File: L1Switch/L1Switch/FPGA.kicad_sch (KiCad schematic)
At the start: 34 parts, among them J11 Conn_01x06_Male, U1 XC7A35T-FTG256, X1 LFSPXO076034CUTT

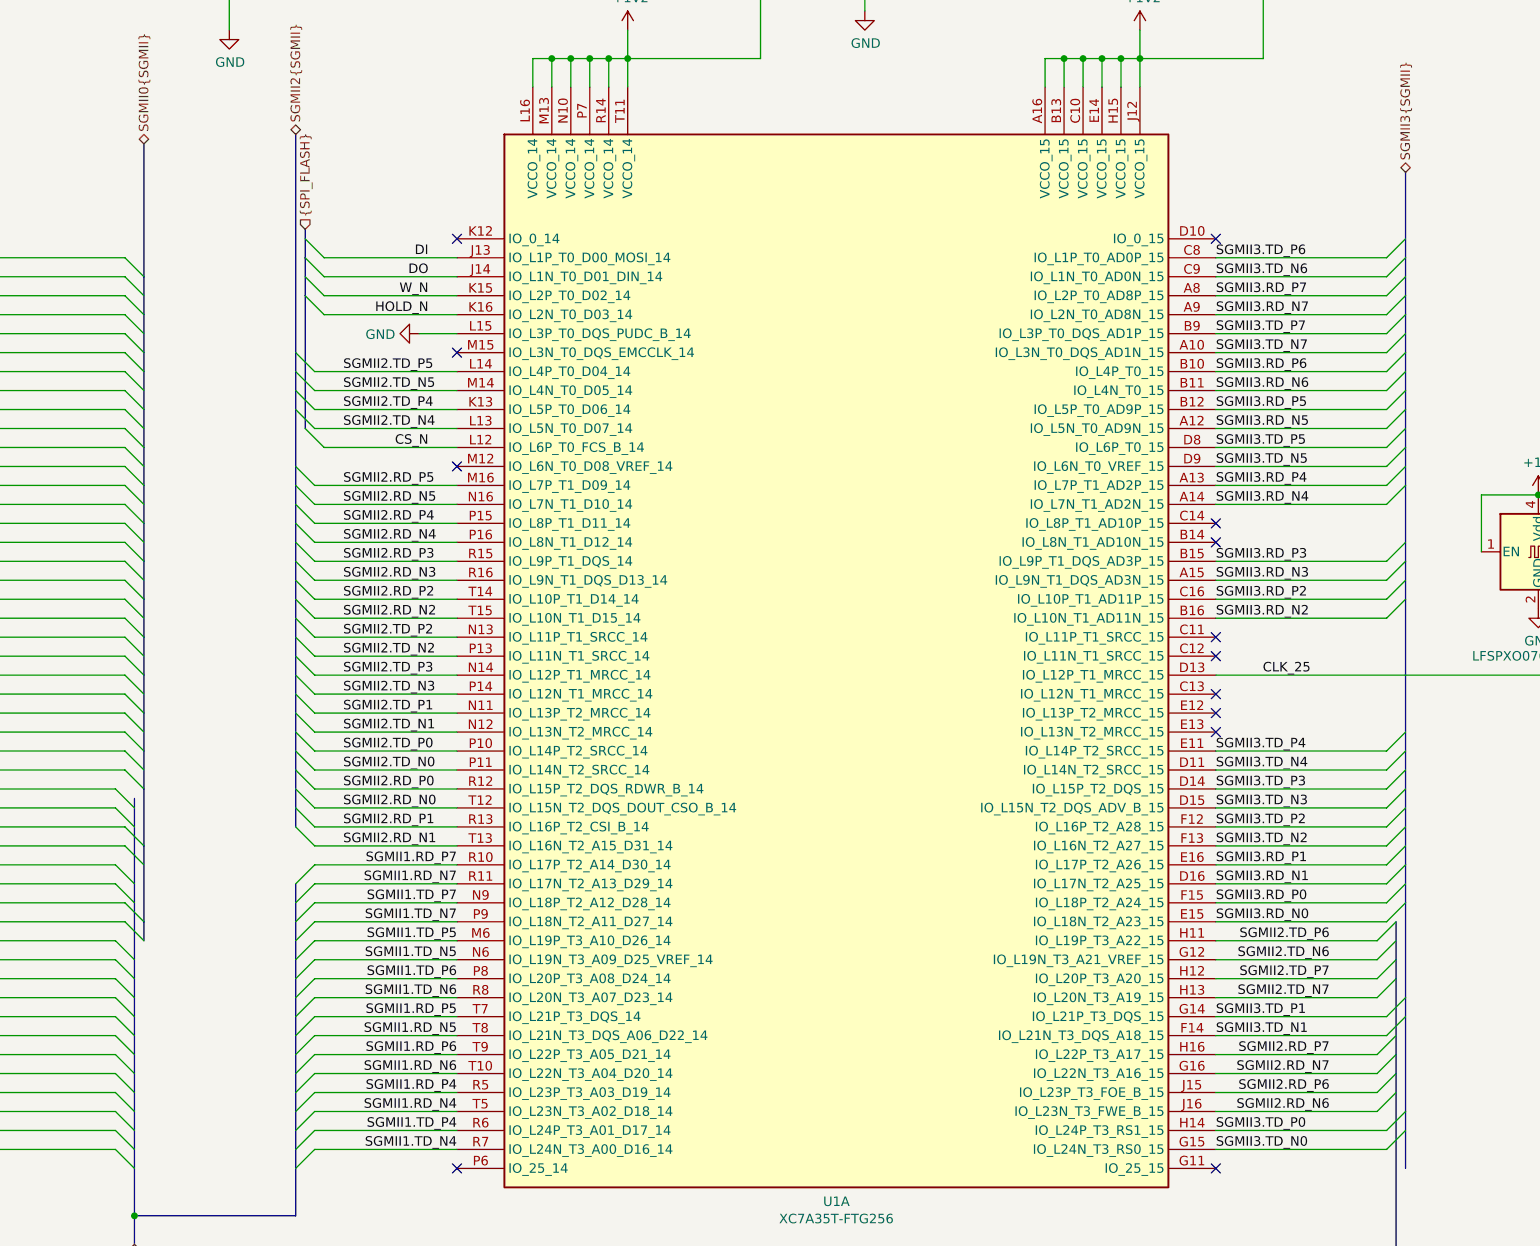
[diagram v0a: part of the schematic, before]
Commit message: Swap fan connector orientation. Add PU/PD for JTAG pins.
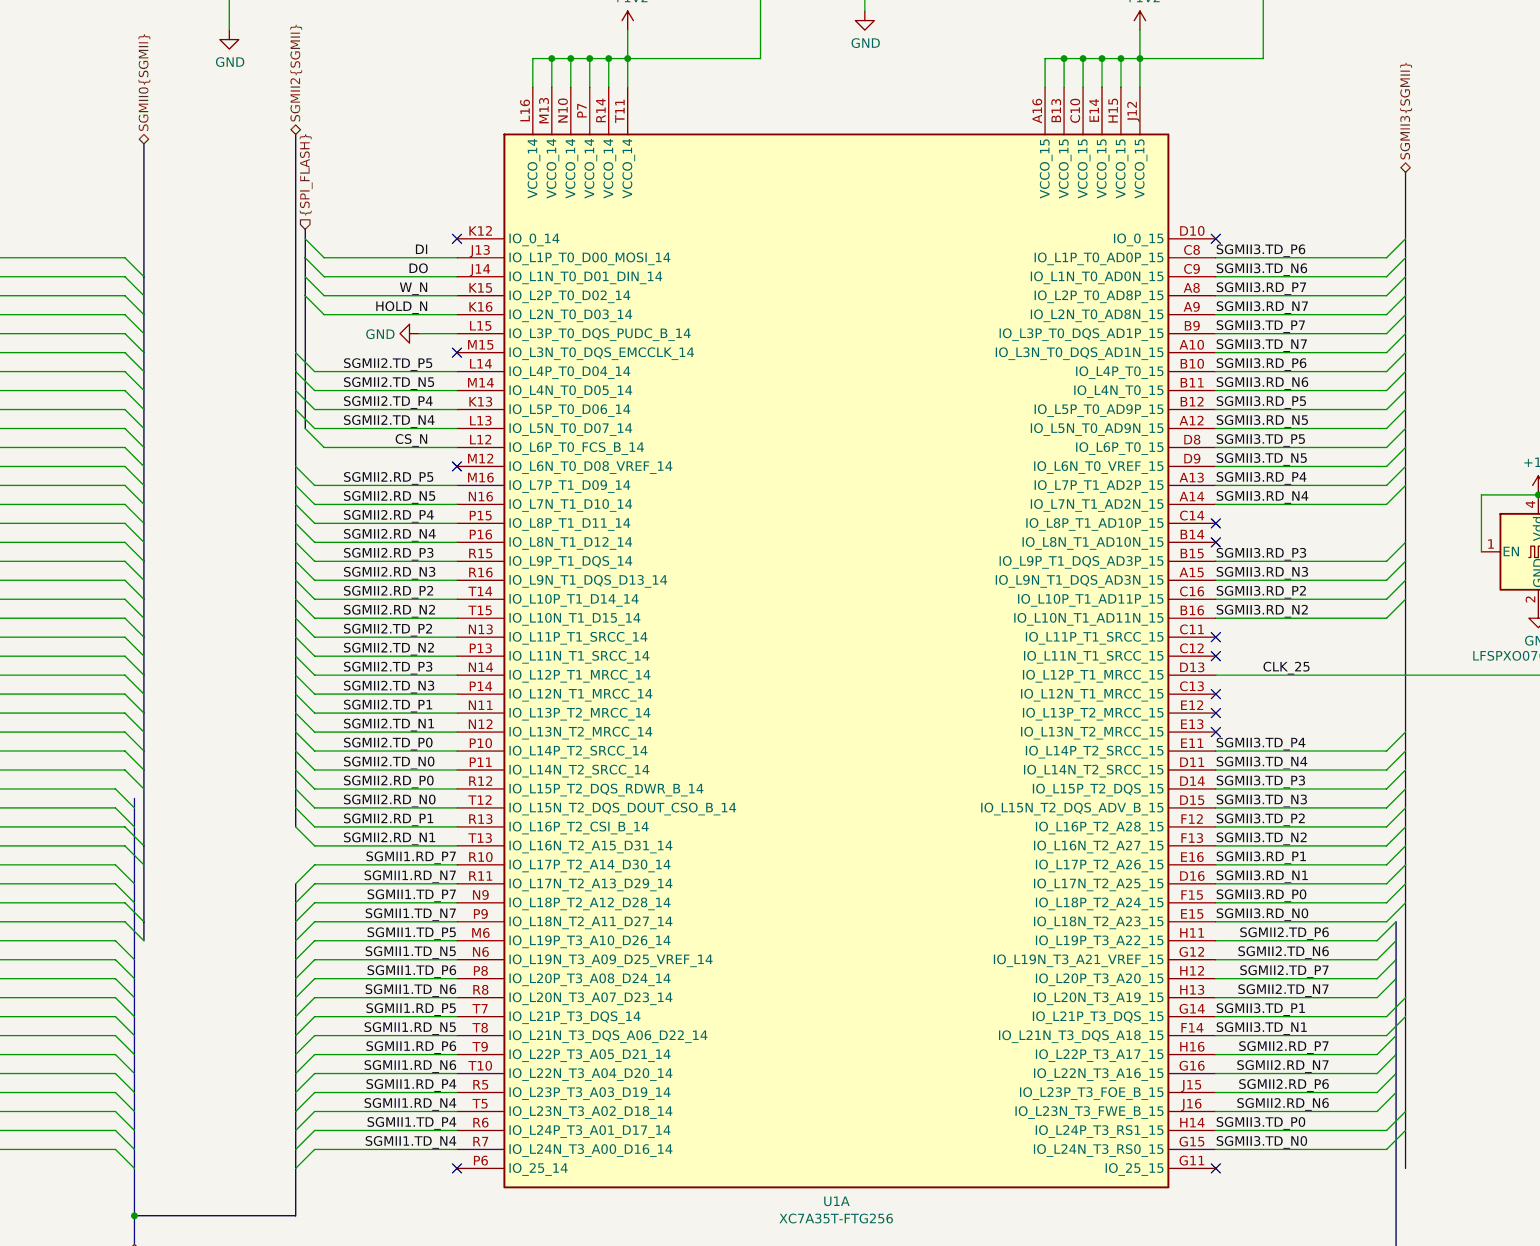
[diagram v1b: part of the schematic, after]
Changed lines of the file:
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@@
   (junction (at 414.02 125.73))
   (junction (at 213.36 198.12))
+  (no_connect (at 177.8 191.77))
+  (no_connect (at 46.99 114.3))
+  (no_connect (at 76.2 107.95))
+  (no_connect (at 256.54 67.31))
+  (no_connect (at 256.54 82.55))
+  (no_connect (at 76.2 115.57))
+  (no_connect (at 358.14 128.27))
+  (no_connect (at 358.14 105.41))
+  (no_connect (at 76.2 102.87))
+  (no_connect (at 358.14 107.95))
+  (no_connect (at 358.14 191.77))
+  (no_connect (at 76.2 105.41))
+  (no_connect (at 46.99 124.46))
+  (no_connect (at 256.54 191.77))
+  (no_connect (at 358.14 130.81))
+  (no_connect (at 46.99 116.84))
+  (no_connect (at 358.14 123.19))
+  (no_connect (at 358.14 120.65))
+  (no_connect (at 358.14 133.35))
+  (no_connect (at 358.14 67.31))
+  (no_connect (at 256.54 97.79))
   (no_connect (at 177.8 67.31))
-  (no_connect (at 358.14 128.27))
-  (no_connect (at 76.2 102.87))
-  (no_connect (at 76.2 105.41))
-  (no_connect (at 256.54 67.31))
-  (no_connect (at 76.2 107.95))
-  (no_connect (at 358.14 105.41))
-  (no_connect (at 46.99 114.3))
-  (no_connect (at 76.2 115.57))
-  (no_connect (at 358.14 133.35))
-  (no_connect (at 358.14 120.65))
-  (no_connect (at 256.54 82.55))
-  (no_connect (at 358.14 123.19))
-  (no_connect (at 256.54 191.77))
-  (no_connect (at 46.99 116.84))
-  (no_connect (at 46.99 124.46))
-  (no_connect (at 358.14 107.95))
-  (no_connect (at 358.14 130.81))
-  (no_connect (at 358.14 191.77))
-  (no_connect (at 177.8 191.77))
-  (no_connect (at 256.54 97.79))
-  (no_connect (at 358.14 67.31))
   (bus_entry (at 210.82 140.97) (size 2.54 2.54))
   (bus_entry (at 210.82 143.51) (size 2.54 2.54))
@@
     (stroke (width 0) (type solid) (color 0 0 0 0))
   )
-  (bus (pts (xy 213.36 171.45) (xy 213.36 173.99))
-    (stroke (width 0) (type solid) (color 0 0 0 0))
-  )
-  (bus (pts (xy 213.36 173.99) (xy 213.36 179.07))
-    (stroke (width 0) (type solid) (color 0 0 0 0))
-  )
-  (bus (pts (xy 213.36 179.07) (xy 213.36 184.15))
+  (bus (pts (xy 213.36 171.45) (xy 213.36 176.53))
+    (stroke (width 0) (type solid) (color 0 0 0 0))
+  )
+  (bus (pts (xy 213.36 176.53) (xy 213.36 181.61))
+    (stroke (width 0) (type solid) (color 0 0 0 0))
+  )
+  (bus (pts (xy 213.36 181.61) (xy 213.36 184.15))
     (stroke (width 0) (type solid) (color 0 0 0 0))
   )
@@
     (stroke (width 0) (type solid) (color 0 0 0 0))
   )
-  (bus (pts (xy 214.63 135.89) (xy 214.63 140.97))
-    (stroke (width 0) (type solid) (color 0 0 0 0))
-  )
-  (bus (pts (xy 214.63 140.97) (xy 214.63 148.59))
+  (bus (pts (xy 214.63 135.89) (xy 214.63 138.43))
+    (stroke (width 0) (type solid) (color 0 0 0 0))
+  )
+  (bus (pts (xy 214.63 138.43) (xy 214.63 148.59))
     (stroke (width 0) (type solid) (color 0 0 0 0))
   )
@@
     (stroke (width 0) (type solid) (color 0 0 0 0))
   )
-  (bus (pts (xy 234.95 53.34) (xy 234.95 82.55))
-    (stroke (width 0) (type solid) (color 0 0 0 0))
-  )
-  (bus (pts (xy 234.95 82.55) (xy 234.95 87.63))
-    (stroke (width 0) (type solid) (color 0 0 0 0))
-  )
-  (bus (pts (xy 234.95 87.63) (xy 234.95 97.79))
-    (stroke (width 0) (type solid) (color 0 0 0 0))
-  )
-  (bus (pts (xy 234.95 97.79) (xy 234.95 100.33))
-    (stroke (width 0) (type solid) (color 0 0 0 0))
-  )
-  (bus (pts (xy 234.95 100.33) (xy 234.95 105.41))
-    (stroke (width 0) (type solid) (color 0 0 0 0))
-  )
-  (bus (pts (xy 234.95 105.41) (xy 234.95 110.49))
-    (stroke (width 0) (type solid) (color 0 0 0 0))
-  )
-  (bus (pts (xy 234.95 110.49) (xy 234.95 115.57))
-    (stroke (width 0) (type solid) (color 0 0 0 0))
-  )
-  (bus (pts (xy 234.95 115.57) (xy 234.95 120.65))
-    (stroke (width 0) (type solid) (color 0 0 0 0))
-  )
-  (bus (pts (xy 234.95 120.65) (xy 234.95 125.73))
-    (stroke (width 0) (type solid) (color 0 0 0 0))
-  )
-  (bus (pts (xy 234.95 125.73) (xy 234.95 130.81))
-    (stroke (width 0) (type solid) (color 0 0 0 0))
-  )
-  (bus (pts (xy 234.95 130.81) (xy 234.95 133.35))
-    (stroke (width 0) (type solid) (color 0 0 0 0))
-  )
-  (bus (pts (xy 234.95 133.35) (xy 234.95 138.43))
-    (stroke (width 0) (type solid) (color 0 0 0 0))
-  )
-  (bus (pts (xy 234.95 138.43) (xy 234.95 143.51))
-    (stroke (width 0) (type solid) (color 0 0 0 0))
-  )
-  (bus (pts (xy 234.95 143.51) (xy 234.95 146.05))
+  (bus (pts (xy 234.95 53.34) (xy 234.95 85.09))
+    (stroke (width 0) (type solid) (color 0 0 0 0))
+  )
+  (bus (pts (xy 234.95 85.09) (xy 234.95 90.17))
+    (stroke (width 0) (type solid) (color 0 0 0 0))
+  )
+  (bus (pts (xy 234.95 90.17) (xy 234.95 100.33))
+    (stroke (width 0) (type solid) (color 0 0 0 0))
+  )
+  (bus (pts (xy 234.95 100.33) (xy 234.95 102.87))
+    (stroke (width 0) (type solid) (color 0 0 0 0))
+  )
+  (bus (pts (xy 234.95 102.87) (xy 234.95 107.95))
+    (stroke (width 0) (type solid) (color 0 0 0 0))
+  )
+  (bus (pts (xy 234.95 107.95) (xy 234.95 113.03))
+    (stroke (width 0) (type solid) (color 0 0 0 0))
+  )
+  (bus (pts (xy 234.95 113.03) (xy 234.95 118.11))
+    (stroke (width 0) (type solid) (color 0 0 0 0))
+  )
+  (bus (pts (xy 234.95 118.11) (xy 234.95 123.19))
+    (stroke (width 0) (type solid) (color 0 0 0 0))
+  )
+  (bus (pts (xy 234.95 123.19) (xy 234.95 128.27))
+    (stroke (width 0) (type solid) (color 0 0 0 0))
+  )
+  (bus (pts (xy 234.95 128.27) (xy 234.95 133.35))
+    (stroke (width 0) (type solid) (color 0 0 0 0))
+  )
+  (bus (pts (xy 234.95 133.35) (xy 234.95 135.89))
+    (stroke (width 0) (type solid) (color 0 0 0 0))
+  )
+  (bus (pts (xy 234.95 135.89) (xy 234.95 140.97))
+    (stroke (width 0) (type solid) (color 0 0 0 0))
+  )
+  (bus (pts (xy 234.95 140.97) (xy 234.95 146.05))
     (stroke (width 0) (type solid) (color 0 0 0 0))
   )
@@
     (stroke (width 0) (type solid) (color 0 0 0 0))
   )
-  (bus (pts (xy 383.54 151.13) (xy 383.54 156.21))
-    (stroke (width 0) (type solid) (color 0 0 0 0))
-  )
-  (bus (pts (xy 383.54 156.21) (xy 383.54 168.91))
-    (stroke (width 0) (type solid) (color 0 0 0 0))
-  )
+  (bus (pts (xy 383.54 151.13) (xy 383.54 153.67))
+    (stroke (width 0) (type solid) (color 0 0 0 0))
+  )
+  (bus (pts (xy 383.54 153.67) (xy 383.54 168.91))
+    (stroke (width 0) (type solid) (color 0 0 0 0))
+  )

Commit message: Update RJ45 pinout on schematic and partial layout update.
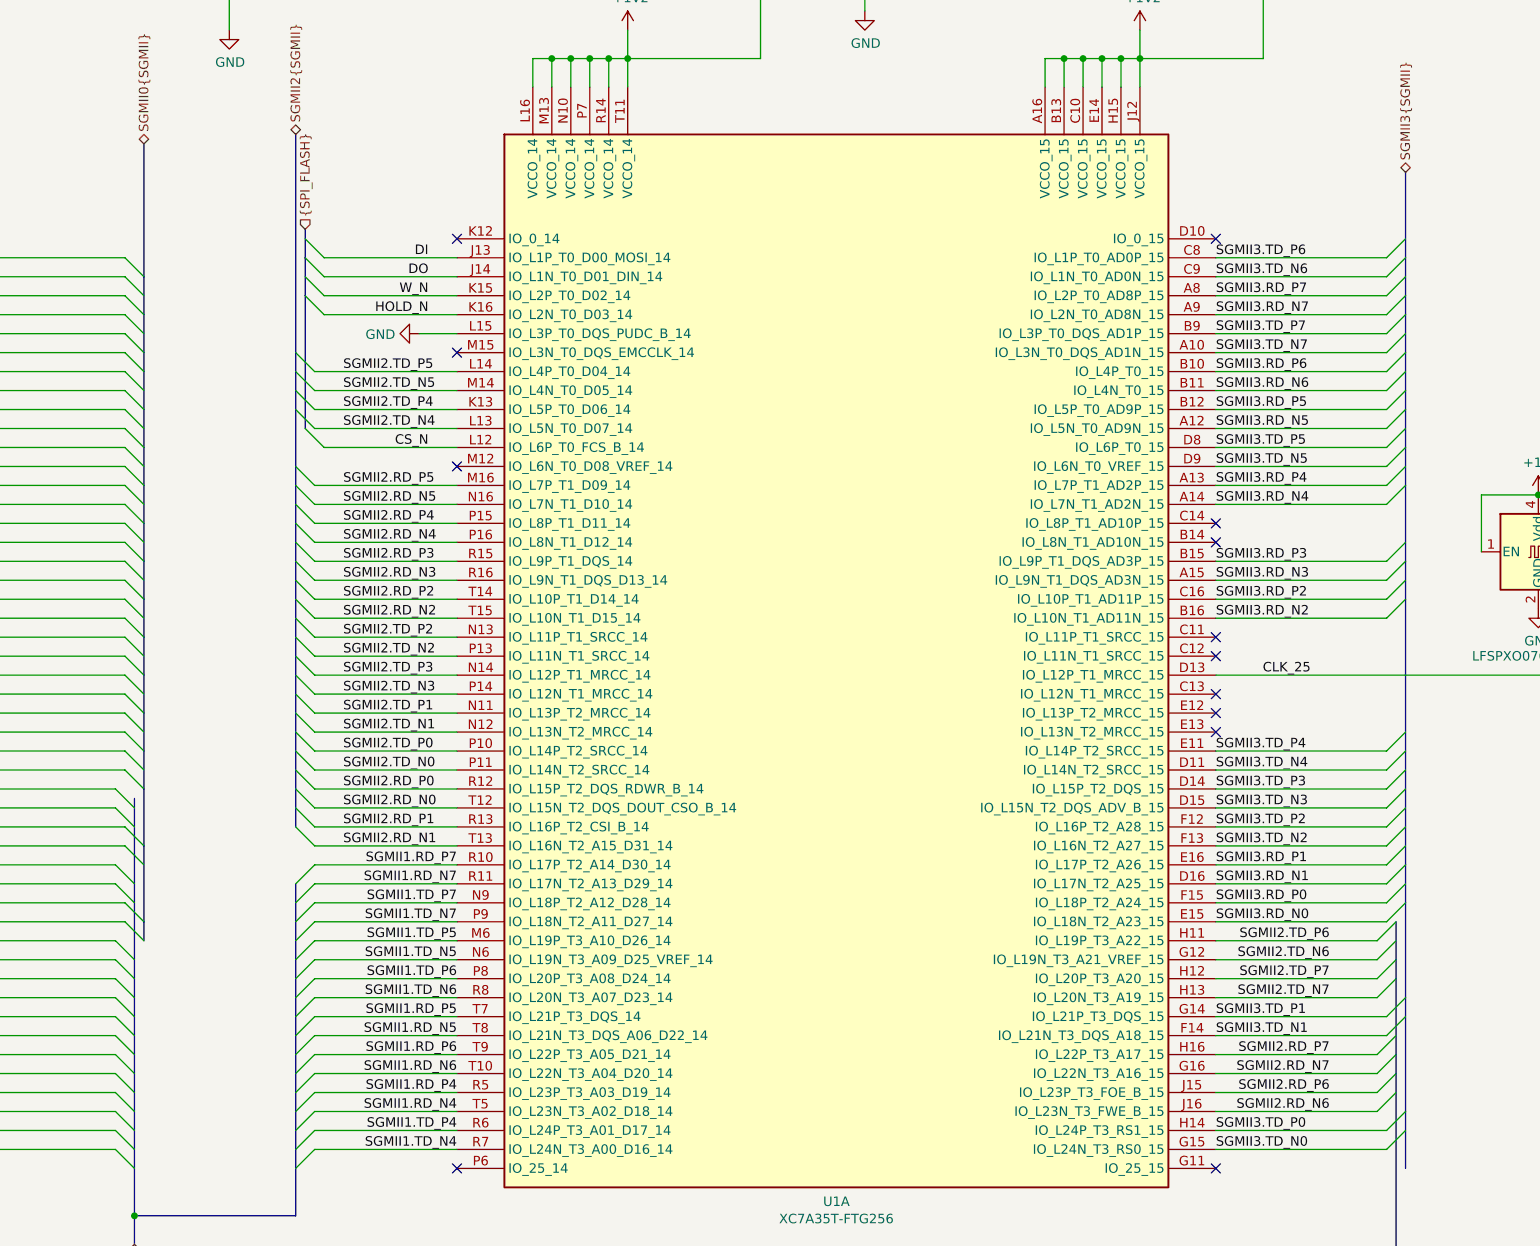
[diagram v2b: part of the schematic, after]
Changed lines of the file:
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@@
 (kicad_sch (version 20200608) (host eeschema "5.99.0-unknown-1973153~101~ubuntu20.04.1")
-  (page 2 12)
+  (page 1 12)
   (paper "B")
   (bus_alias "MAC1_SGMII" (members ))
@@
   (junction (at 414.02 125.73))
   (junction (at 213.36 198.12))
+  (no_connect (at 358.14 105.41))
+  (no_connect (at 358.14 123.19))
+  (no_connect (at 358.14 191.77))
+  (no_connect (at 76.2 102.87))
+  (no_connect (at 76.2 115.57))
+  (no_connect (at 177.8 67.31))
+  (no_connect (at 358.14 130.81))
+  (no_connect (at 256.54 67.31))
+  (no_connect (at 46.99 114.3))
+  (no_connect (at 358.14 133.35))
+  (no_connect (at 76.2 107.95))
+  (no_connect (at 358.14 120.65))
+  (no_connect (at 256.54 97.79))
   (no_connect (at 177.8 191.77))
-  (no_connect (at 46.99 114.3))
-  (no_connect (at 76.2 107.95))
-  (no_connect (at 256.54 67.31))
+  (no_connect (at 256.54 191.77))
+  (no_connect (at 76.2 105.41))
+  (no_connect (at 46.99 116.84))
+  (no_connect (at 358.14 128.27))
+  (no_connect (at 358.14 67.31))
+  (no_connect (at 46.99 124.46))
   (no_connect (at 256.54 82.55))
-  (no_connect (at 76.2 115.57))
-  (no_connect (at 358.14 128.27))
-  (no_connect (at 358.14 105.41))
-  (no_connect (at 76.2 102.87))
   (no_connect (at 358.14 107.95))
-  (no_connect (at 358.14 191.77))
-  (no_connect (at 76.2 105.41))
-  (no_connect (at 46.99 124.46))
-  (no_connect (at 256.54 191.77))
-  (no_connect (at 358.14 130.81))
-  (no_connect (at 46.99 116.84))
-  (no_connect (at 358.14 123.19))
-  (no_connect (at 358.14 120.65))
-  (no_connect (at 358.14 133.35))
-  (no_connect (at 358.14 67.31))
-  (no_connect (at 256.54 97.79))
-  (no_connect (at 177.8 67.31))
   (bus_entry (at 210.82 140.97) (size 2.54 2.54))
   (bus_entry (at 210.82 143.51) (size 2.54 2.54))
@@
     (stroke (width 0) (type solid) (color 0 0 0 0))
   )
-  (bus (pts (xy 213.36 171.45) (xy 213.36 176.53))
-    (stroke (width 0) (type solid) (color 0 0 0 0))
-  )
-  (bus (pts (xy 213.36 176.53) (xy 213.36 181.61))
-    (stroke (width 0) (type solid) (color 0 0 0 0))
-  )
-  (bus (pts (xy 213.36 181.61) (xy 213.36 184.15))
+  (bus (pts (xy 213.36 171.45) (xy 213.36 173.99))
+    (stroke (width 0) (type solid) (color 0 0 0 0))
+  )
+  (bus (pts (xy 213.36 173.99) (xy 213.36 179.07))
+    (stroke (width 0) (type solid) (color 0 0 0 0))
+  )
+  (bus (pts (xy 213.36 179.07) (xy 213.36 184.15))
     (stroke (width 0) (type solid) (color 0 0 0 0))
   )
@@
     (stroke (width 0) (type solid) (color 0 0 0 0))
   )
-  (bus (pts (xy 214.63 135.89) (xy 214.63 138.43))
-    (stroke (width 0) (type solid) (color 0 0 0 0))
-  )
-  (bus (pts (xy 214.63 138.43) (xy 214.63 148.59))
+  (bus (pts (xy 214.63 135.89) (xy 214.63 140.97))
+    (stroke (width 0) (type solid) (color 0 0 0 0))
+  )
+  (bus (pts (xy 214.63 140.97) (xy 214.63 148.59))
     (stroke (width 0) (type solid) (color 0 0 0 0))
   )
@@
     (stroke (width 0) (type solid) (color 0 0 0 0))
   )
-  (bus (pts (xy 234.95 53.34) (xy 234.95 85.09))
-    (stroke (width 0) (type solid) (color 0 0 0 0))
-  )
-  (bus (pts (xy 234.95 85.09) (xy 234.95 90.17))
-    (stroke (width 0) (type solid) (color 0 0 0 0))
-  )
-  (bus (pts (xy 234.95 90.17) (xy 234.95 100.33))
-    (stroke (width 0) (type solid) (color 0 0 0 0))
-  )
-  (bus (pts (xy 234.95 100.33) (xy 234.95 102.87))
-    (stroke (width 0) (type solid) (color 0 0 0 0))
-  )
-  (bus (pts (xy 234.95 102.87) (xy 234.95 107.95))
+  (bus (pts (xy 234.95 53.34) (xy 234.95 82.55))
+    (stroke (width 0) (type solid) (color 0 0 0 0))
+  )
+  (bus (pts (xy 234.95 82.55) (xy 234.95 87.63))
+    (stroke (width 0) (type solid) (color 0 0 0 0))
+  )
+  (bus (pts (xy 234.95 87.63) (xy 234.95 97.79))
+    (stroke (width 0) (type solid) (color 0 0 0 0))
+  )
+  (bus (pts (xy 234.95 97.79) (xy 234.95 100.33))
+    (stroke (width 0) (type solid) (color 0 0 0 0))
+  )
+  (bus (pts (xy 234.95 100.33) (xy 234.95 105.41))
+    (stroke (width 0) (type solid) (color 0 0 0 0))
+  )
+  (bus (pts (xy 234.95 105.41) (xy 234.95 107.95))
     (stroke (width 0) (type solid) (color 0 0 0 0))
   )
@@
     (stroke (width 0) (type solid) (color 0 0 0 0))
   )
-  (bus (pts (xy 383.54 151.13) (xy 383.54 153.67))
-    (stroke (width 0) (type solid) (color 0 0 0 0))
-  )
-  (bus (pts (xy 383.54 153.67) (xy 383.54 168.91))
-    (stroke (width 0) (type solid) (color 0 0 0 0))
-  )
+  (bus (pts (xy 383.54 151.13) (xy 383.54 156.21))
+    (stroke (width 0) (type solid) (color 0 0 0 0))
+  )
+  (bus (pts (xy 383.54 156.21) (xy 383.54 168.91))
+    (stroke (width 0) (type solid) (color 0 0 0 0))
+  )
